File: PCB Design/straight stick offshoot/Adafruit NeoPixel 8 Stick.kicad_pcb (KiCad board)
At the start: 2 copper layers, 72.5 x 26.1 mm, 11 parts, among them CN1 1X4SMT, CN2 1X4SMT, CN3 1X4SMT

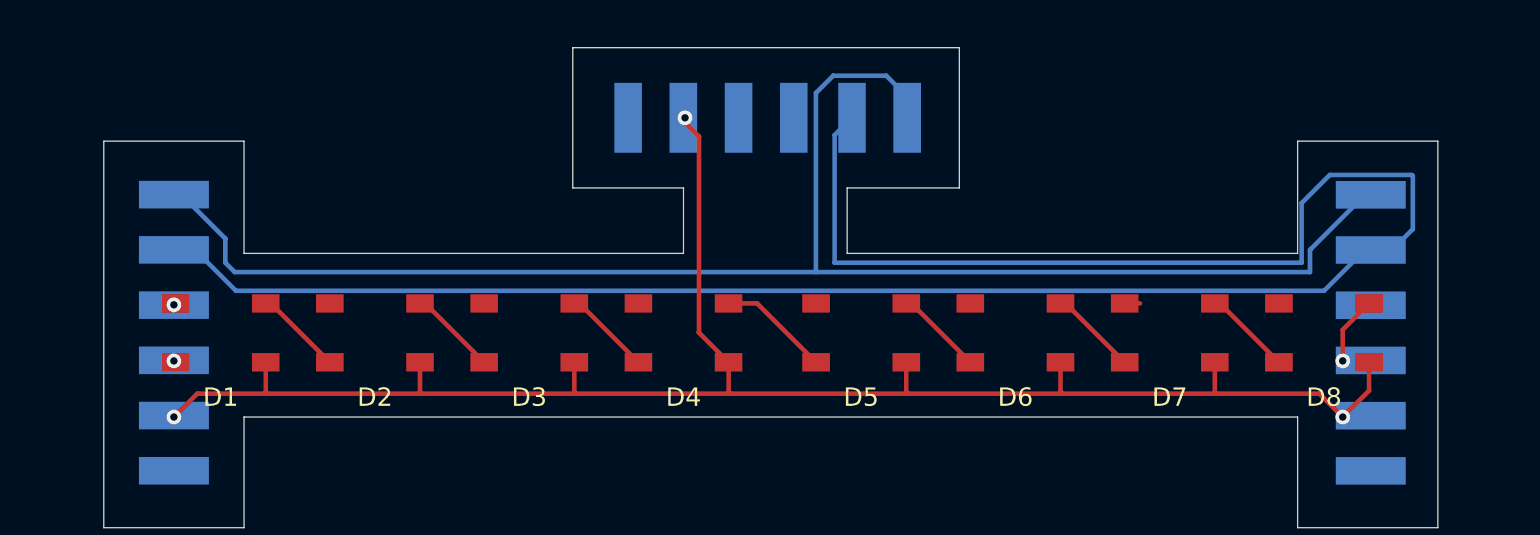
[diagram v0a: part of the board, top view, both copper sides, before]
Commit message: move vias off pads
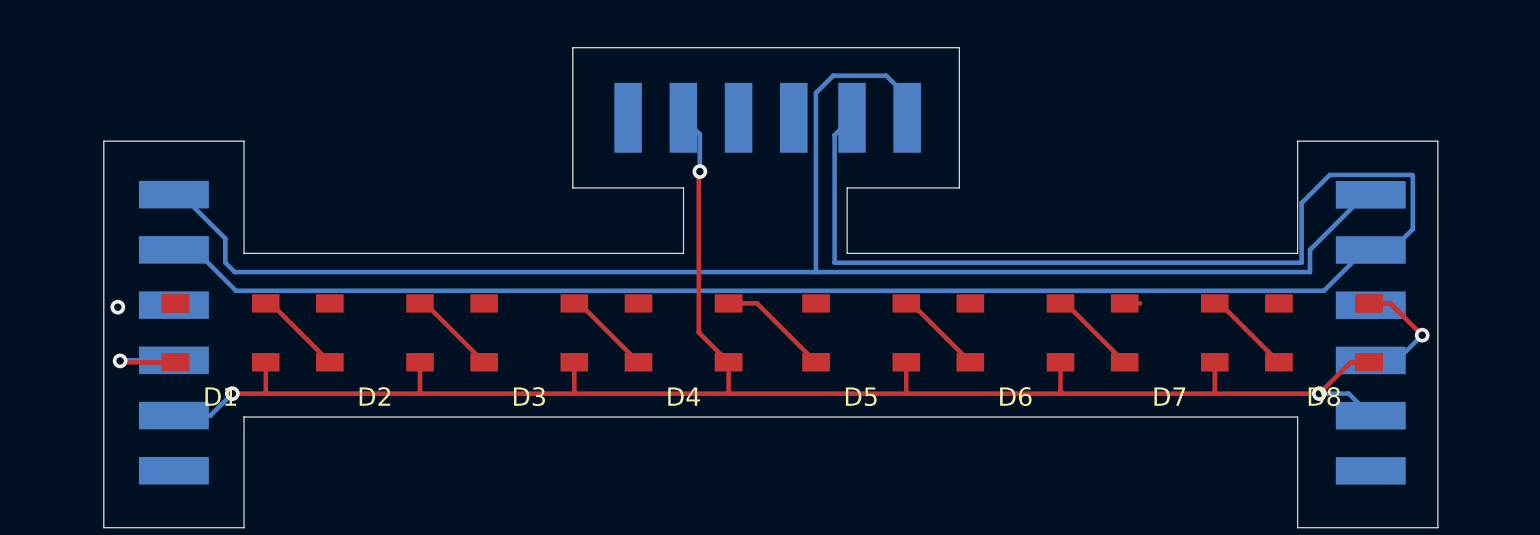
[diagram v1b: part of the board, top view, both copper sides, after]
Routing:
- net Net-(CN2-Pad3): track 0.00 -> 5.98 mm
- net Net-(CN1-Pad4): track 3.72 -> 6.96 mm
- net +5V: track 94.6 -> 95.9 mm
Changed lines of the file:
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@@
   (segment (start 166.026 109.55) (end 166.026 111.162) (width 0.25) (layer "F.Cu") (net 1))
   (segment (start 139.61 111.162) (end 139.7 111.252) (width 0.25) (layer "F.Cu") (net 1))
-  (segment (start 127.508 111.252) (end 131.318 111.252) (width 0.25) (layer "F.Cu") (net 1))
-  (segment (start 189.738 112.522) (end 191.172 111.088) (width 0.25) (layer "F.Cu") (net 1))
   (segment (start 182.79 109.55) (end 182.79 111.162) (width 0.25) (layer "F.Cu") (net 1))
+  (segment (start 129.413 111.252) (end 131.318 111.252) (width 0.25) (layer "F.Cu") (net 1))
   (segment (start 148.082 111.252) (end 156.464 111.252) (width 0.25) (layer "F.Cu") (net 1))
   (segment (start 166.116 111.252) (end 174.498 111.252) (width 0.25) (layer "F.Cu") (net 1))
   (segment (start 156.374 109.55) (end 156.374 111.162) (width 0.25) (layer "F.Cu") (net 1))
   (segment (start 139.7 111.252) (end 148.082 111.252) (width 0.25) (layer "F.Cu") (net 1))
-  (segment (start 126.238 112.522) (end 127.508 111.252) (width 0.25) (layer "F.Cu") (net 1))
   (segment (start 147.992 109.55) (end 147.992 111.162) (width 0.25) (layer "F.Cu") (net 1))
   (segment (start 131.318 111.252) (end 139.7 111.252) (width 0.25) (layer "F.Cu") (net 1))
-  (segment (start 191.172 111.088) (end 191.172 109.55) (width 0.25) (layer "F.Cu") (net 1))
-  (segment (start 154.006 96.266) (end 154.006 96.52) (width 0.25) (layer "F.Cu") (net 1))
-  (segment (start 154.768 97.282) (end 154.768 107.916) (width 0.25) (layer "F.Cu") (net 1))
   (segment (start 156.374 111.162) (end 156.464 111.252) (width 0.25) (layer "F.Cu") (net 1))
-  (segment (start 154.754 107.93) (end 156.374 109.55) (width 0.25) (layer "F.Cu") (net 1))
+  (segment (start 190.17 109.55) (end 191.172 109.55) (width 0.25) (layer "F.Cu") (net 1))
   (segment (start 139.61 109.55) (end 139.61 111.162) (width 0.25) (layer "F.Cu") (net 1))
   (segment (start 182.88 111.252) (end 188.468 111.252) (width 0.25) (layer "F.Cu") (net 1))
-  (segment (start 188.468 111.252) (end 189.738 112.522) (width 0.25) (layer "F.Cu") (net 1))
-  (segment (start 154.006 96.52) (end 154.768 97.282) (width 0.25) (layer "F.Cu") (net 1))
   (segment (start 147.992 111.162) (end 148.082 111.252) (width 0.25) (layer "F.Cu") (net 1))
-  (segment (start 154.768 107.916) (end 154.754 107.93) (width 0.25) (layer "F.Cu") (net 1))
   (segment (start 174.498 111.252) (end 182.88 111.252) (width 0.25) (layer "F.Cu") (net 1))
+  (segment (start 154.754 99.246) (end 154.813 99.187) (width 0.25) (layer "F.Cu") (net 1))
   (segment (start 156.464 111.252) (end 166.116 111.252) (width 0.25) (layer "F.Cu") (net 1))
   (segment (start 166.026 111.162) (end 166.116 111.252) (width 0.25) (layer "F.Cu") (net 1))
   (segment (start 131.228 109.55) (end 131.228 111.162) (width 0.25) (layer "F.Cu") (net 1))
+  (segment (start 156.374 109.55) (end 154.754 107.93) (width 0.25) (layer "F.Cu") (net 1))
   (segment (start 174.408 111.162) (end 174.498 111.252) (width 0.25) (layer "F.Cu") (net 1))
   (segment (start 131.228 111.162) (end 131.318 111.252) (width 0.25) (layer "F.Cu") (net 1))
+  (segment (start 154.754 107.93) (end 154.754 99.246) (width 0.25) (layer "F.Cu") (net 1))
   (segment (start 174.408 109.55) (end 174.408 111.162) (width 0.25) (layer "F.Cu") (net 1))
+  (segment (start 188.468 111.252) (end 190.17 109.55) (width 0.25) (layer "F.Cu") (net 1))
   (segment (start 182.79 111.162) (end 182.88 111.252) (width 0.25) (layer "F.Cu") (net 1))
-  (via (at 126.238 112.522) (size 0.8) (drill 0.4) (layers "F.Cu" "B.Cu") (net 1))
-  (via (at 189.738 112.522) (size 0.8) (drill 0.4) (layers "F.Cu" "B.Cu") (net 1))
-  (via (at 154.006 96.266) (size 0.8) (drill 0.4) (layers "F.Cu" "B.Cu") (net 1))
+  (via (at 129.413 111.252) (size 0.8) (drill 0.4) (layers "F.Cu" "B.Cu") (net 1))
+  (via (at 188.468 111.252) (size 0.8) (drill 0.4) (layers "F.Cu" "B.Cu") (net 1))
+  (via (at 154.813 99.187) (size 0.8) (drill 0.4) (layers "F.Cu" "B.Cu") (net 1))
+  (segment (start 154.813 97.163) (end 154.813 99.187) (width 0.25) (layer "B.Cu") (net 1))
+  (segment (start 153.916 96.266) (end 154.813 97.163) (width 0.25) (layer "B.Cu") (net 1))
+  (segment (start 191.262 112.45) (end 190.064 111.252) (width 0.25) (layer "B.Cu") (net 1))
+  (segment (start 128.223 112.442) (end 129.413 111.252) (width 0.25) (layer "B.Cu") (net 1))
+  (segment (start 190.064 111.252) (end 188.468 111.252) (width 0.25) (layer "B.Cu") (net 1))
+  (segment (start 126.238 112.442) (end 128.223 112.442) (width 0.25) (layer "B.Cu") (net 1))
   (segment (start 178.726 106.35) (end 177.622 106.35) (width 0.25) (layer "F.Cu") (net 2))
-  (via (at 126.238 106.426) (size 0.8) (drill 0.4) (layers "F.Cu" "B.Cu") (net 2))
+  (via (at 123.19 106.553) (size 0.8) (drill 0.4) (layers "F.Cu" "B.Cu") (free) (net 2))
   (segment (start 189.0338 99.3718) (end 187.5068 100.8988) (width 0.25) (layer "B.Cu") (net 3))
   (segment (start 192.412 103.45) (end 193.548 102.314) (width 0.25) (layer "B.Cu") (net 3))
@@
   (segment (start 188.722 105.664) (end 190.936 103.45) (width 0.25) (layer "B.Cu") (net 3))
   (segment (start 127.388 103.442) (end 129.61 105.664) (width 0.25) (layer "B.Cu") (net 3))
-  (via (at 126.238 109.474) (size 0.8) (drill 0.4) (layers "F.Cu" "B.Cu") (net 4))
+  (segment (start 123.393 109.55) (end 123.317 109.474) (width 0.25) (layer "F.Cu") (net 4))
+  (segment (start 126.328 109.55) (end 123.393 109.55) (width 0.25) (layer "F.Cu") (net 4))
+  (via (at 123.317 109.474) (size 0.8) (drill 0.4) (layers "F.Cu" "B.Cu") (net 4))
+  (segment (start 126.238 109.442) (end 123.349 109.442) (width 0.25) (layer "B.Cu") (net 4))
+  (segment (start 123.349 109.442) (end 123.317 109.474) (width 0.25) (layer "B.Cu") (net 4))
   (segment (start 131.51 106.35) (end 134.71 109.55) (width 0.25) (layer "F.Cu") (net 5))
   (segment (start 139.892 106.35) (end 143.092 109.55) (width 0.25) (layer "F.Cu") (net 6))
@@
   (segment (start 174.69 106.35) (end 177.89 109.55) (width 0.25) (layer "F.Cu") (net 10))
   (segment (start 183.072 106.35) (end 186.272 109.55) (width 0.25) (layer "F.Cu") (net 11))
-  (segment (start 189.738 109.474) (end 189.738 107.784) (width 0.25) (layer "F.Cu") (net 12))
-  (segment (start 189.738 107.784) (end 191.172 106.35) (width 0.25) (layer "F.Cu") (net 12))
-  (via (at 189.738 109.474) (size 0.8) (drill 0.4) (layers "F.Cu" "B.Cu") (net 12))
+  (segment (start 192.329 106.35) (end 194.056 108.077) (width 0.25) (layer "F.Cu") (net 12))
+  (segment (start 191.172 106.35) (end 192.329 106.35) (width 0.25) (layer "F.Cu") (net 12))
+  (via (at 194.056 108.077) (size 0.8) (drill 0.4) (layers "F.Cu" "B.Cu") (net 12))
+  (segment (start 192.683 109.45) (end 194.056 108.077) (width 0.25) (layer "B.Cu") (net 12))
+  (segment (start 191.262 109.45) (end 192.683 109.45) (width 0.25) (layer "B.Cu") (net 12))
   (segment (start 187.96 103.4456) (end 190.9556 100.45) (width 0.25) (layer "B.Cu") (net 13))
   (segment (start 164.94 93.98) (end 162.0556 93.98) (width 0.25) (layer "B.Cu") (net 13))
